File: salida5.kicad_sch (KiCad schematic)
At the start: 7 parts

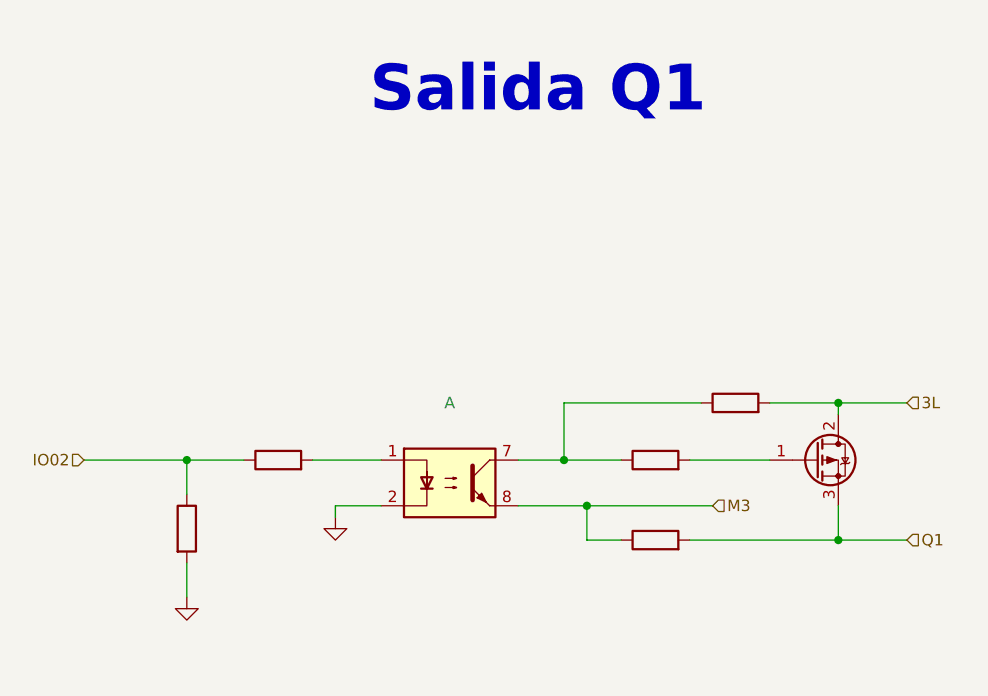
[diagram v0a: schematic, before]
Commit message: add salidas separadas 4,5,6
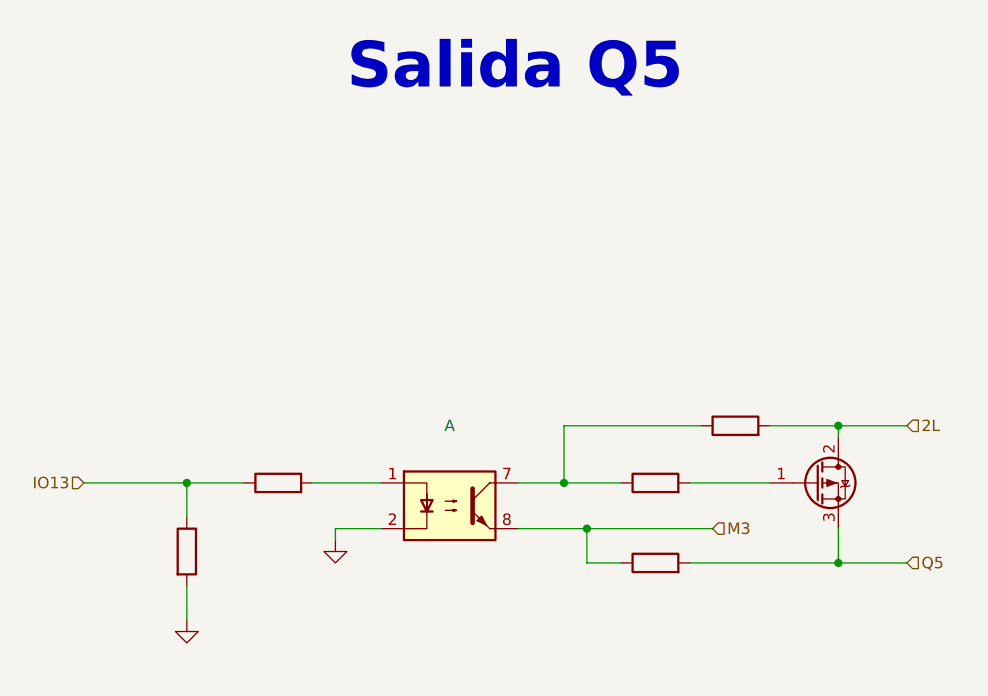
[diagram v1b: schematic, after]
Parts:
- removed ? (x5): (no value), symbol Device:R
- removed ?: (no value), symbol Transistor_FET:FQP27P06
- removed ?: (no value), symbol Isolator:ILD74
- added ? (x5): (no value), symbol Device:R
- added ?: (no value), symbol Isolator:ILD74
- added ?: (no value), symbol Transistor_FET:FQP27P06
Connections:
- net GND: now also ?.2, ?.2
- net M3: now also ?.1, ?.8
- new net: ?.1, ?.1, ?.7
- new net: ?.1, ?.2
- new net: ?.1 (G), ?.2
- new net 2L: ?.2, ?.2 (D)
- new net IO13: ?.1, ?.1
- new net Q5: ?.2, ?.3 (S)
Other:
- note added: "Salida Q5"
- note removed: "Salida Q1"

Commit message: add entradas separadas
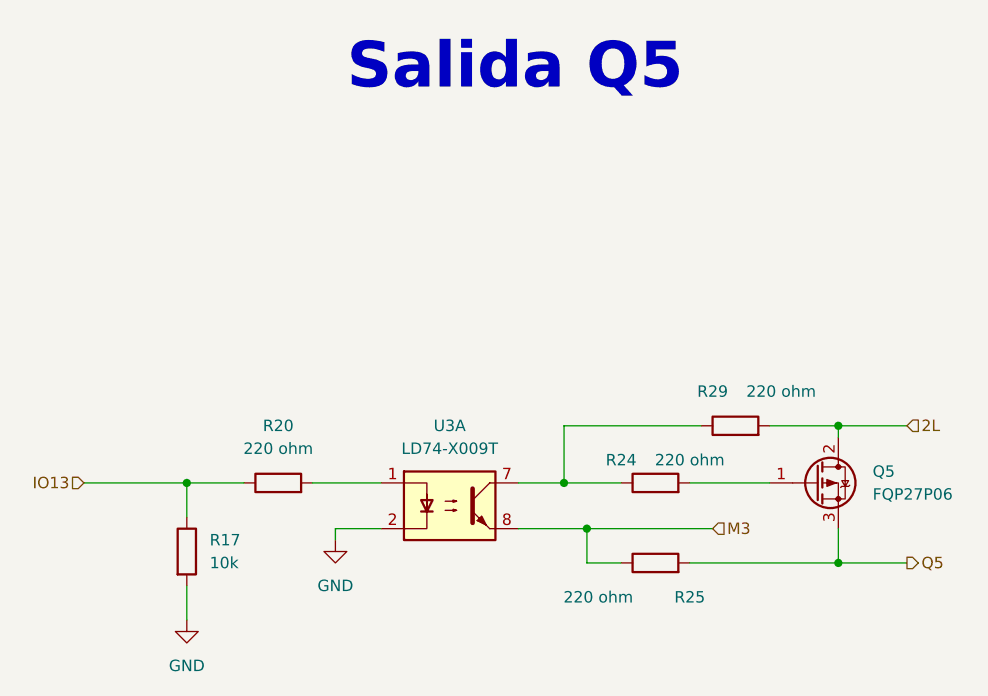
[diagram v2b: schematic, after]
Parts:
- Q5: renamed from ?; value (none) -> FQP27P06; footprint (none) -> Package_TO_SOT_SMD:TO-252-3_TabPin2
- R17: renamed from ?; value (none) -> 10k; footprint (none) -> Resistor_SMD:R_0603_1608Metric
- R20, R24, R25, R29: renamed from ?; value (none) -> 220 ohm; footprint (none) -> Resistor_SMD:R_0603_1608Metric
- U3: renamed from ?; value (none) -> LD74-X009T; footprint (none) -> Package_DIP:DIP-8_W8.89mm_SMDSocket_LongPads
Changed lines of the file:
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@@
-(kicad_sch (version 20220929) (generator eeschema)
+(kicad_sch (version 20221004) (generator eeschema)
   (paper "A4" portrait)
+  (title_block
+    (rev "José Luis Laica")
+  )
   (junction (at 140.97 115.57) (diameter 0) (color 0 0 0 0)
   )
@@
     (effects (font (size 1.27 1.27)) (justify left))
   )
-  (hierarchical_label "Q5" (shape input) (at 148.59 130.81 0) (fields_autoplaced)
+  (hierarchical_label "Q5" (shape output) (at 148.59 130.81 0) (fields_autoplaced)
     (effects (font (size 1.27 1.27)) (justify left))
   )
   (symbol (lib_id "power:GND") (at 68.58 137.16 0) (unit 1)
     (in_bom yes) (on_board yes) (dnp no) (fields_autoplaced)
-    (default_instance (reference "") (unit 1) (value "") (footprint ""))
-    (property "Reference" "" (at 68.58 143.51 0)
-      (effects (font (size 1.27 1.27)) hide)
-    )
-    (property "Value" "" (at 68.58 142.24 0)
+    (property "Reference" "#PWR012" (at 68.58 143.51 0)
+      (effects (font (size 1.27 1.27)) hide)
+    )
+    (property "Value" "GND" (at 68.58 142.24 0)
       (effects (font (size 1.27 1.27)))
     )
@@
     )
     (pin "1")
+    (instances
+      (project "PLC 32 V2"
+        (path "/d17a54f1-6eda-453f-95e1-42a53b02a1c3/64b407cd-5d00-473d-9ef6-2525490a4831"
+          (reference "#PWR012") (unit 1) (value "GND") (footprint "")
+        )
+      )
+    )
   )
   (symbol (lib_id "Device:R") (at 68.58 129.54 0) (unit 1)
     (in_bom yes) (on_board yes) (dnp no) (fields_autoplaced)
-    (default_instance (reference "") (unit 1) (value "") (footprint ""))
-    (property "Reference" "" (at 71.12 128.2699 0)
-      (effects (font (size 1.27 1.27)) (justify left))
-    )
-    (property "Value" "" (at 71.12 130.8099 0)
-      (effects (font (size 1.27 1.27)) (justify left))
-    )
-    (property "Footprint" "" (at 66.802 129.54 90)
+    (property "Reference" "R17" (at 71.12 128.2699 0)
+      (effects (font (size 1.27 1.27)) (justify left))
+    )
+    (property "Value" "10k" (at 71.12 130.8099 0)
+      (effects (font (size 1.27 1.27)) (justify left))
+    )
+    (property "Footprint" "Resistor_SMD:R_0603_1608Metric" (at 66.802 129.54 90)
       (effects (font (size 1.27 1.27)) hide)
     )
@@
     (pin "1")
     (pin "2")
+    (instances
+      (project "PLC 32 V2"
+        (path "/d17a54f1-6eda-453f-95e1-42a53b02a1c3/64b407cd-5d00-473d-9ef6-2525490a4831"
+          (reference "R17") (unit 1) (value "10k") (footprint "Resistor_SMD:R_0603_1608Metric")
+        )
+      )
+    )
   )
   (symbol (lib_id "Device:R") (at 120.65 130.81 90) (unit 1)
     (in_bom yes) (on_board yes) (dnp no)
-    (default_instance (reference "") (unit 1) (value "") (footprint ""))
-    (property "Reference" "" (at 124.46 134.62 90)
-      (effects (font (size 1.27 1.27)))
-    )
-    (property "Value" "" (at 114.3 134.62 90)
-      (effects (font (size 1.27 1.27)))
-    )
-    (property "Footprint" "" (at 120.65 132.588 90)
+    (property "Reference" "R25" (at 124.46 134.62 90)
+      (effects (font (size 1.27 1.27)))
+    )
+    (property "Value" "220 ohm" (at 114.3 134.62 90)
+      (effects (font (size 1.27 1.27)))
+    )
+    (property "Footprint" "Resistor_SMD:R_0603_1608Metric" (at 120.65 132.588 90)
       (effects (font (size 1.27 1.27)) hide)
     )
@@
     (pin "1")
     (pin "2")
+    (instances
+      (project "PLC 32 V2"
+        (path "/d17a54f1-6eda-453f-95e1-42a53b02a1c3/64b407cd-5d00-473d-9ef6-2525490a4831"
+          (reference "R25") (unit 1) (value "220 ohm") (footprint "Resistor_SMD:R_0603_1608Metric")
+        )
+      )
+    )
   )
   (symbol (lib_id "Device:R") (at 129.54 115.57 90) (unit 1)
     (in_bom yes) (on_board yes) (dnp no)
-    (default_instance (reference "") (unit 1) (value "") (footprint ""))
-    (property "Reference" "" (at 127 111.76 90)
-      (effects (font (size 1.27 1.27)))
-    )
-    (property "Value" "" (at 134.62 111.76 90)
-      (effects (font (size 1.27 1.27)))
-    )
-    (property "Footprint" "" (at 129.54 117.348 90)
+    (property "Reference" "R29" (at 127 111.76 90)
+      (effects (font (size 1.27 1.27)))
+    )
+    (property "Value" "220 ohm" (at 134.62 111.76 90)
+      (effects (font (size 1.27 1.27)))
+    )
+    (property "Footprint" "Resistor_SMD:R_0603_1608Metric" (at 129.54 117.348 90)
       (effects (font (size 1.27 1.27)) hide)
     )
@@
     (pin "1")
     (pin "2")
+    (instances
+      (project "PLC 32 V2"
+        (path "/d17a54f1-6eda-453f-95e1-42a53b02a1c3/64b407cd-5d00-473d-9ef6-2525490a4831"
+          (reference "R29") (unit 1) (value "220 ohm") (footprint "Resistor_SMD:R_0603_1608Metric")
+        )
+      )
+    )
   )
   (symbol (lib_id "Isolator:ILD74") (at 97.79 124.46 0) (unit 1)
     (in_bom yes) (on_board yes) (dnp no) (fields_autoplaced)
-    (default_instance (reference "") (unit 1) (value "") (footprint ""))
-    (property "Reference" "" (at 97.79 115.57 0)
-      (effects (font (size 1.27 1.27)))
-    )
-    (property "Value" "" (at 97.79 118.11 0)
-      (effects (font (size 1.27 1.27)))
-    )
-    (property "Footprint" "" (at 92.71 129.54 0)
+    (property "Reference" "U3" (at 97.79 115.57 0)
+      (effects (font (size 1.27 1.27)))
+    )
+    (property "Value" "LD74-X009T" (at 97.79 118.11 0)
+      (effects (font (size 1.27 1.27)))
+    )
+    (property "Footprint" "Package_DIP:DIP-8_W8.89mm_SMDSocket_LongPads" (at 92.71 129.54 0)
       (effects (font (size 1.27 1.27) italic) (justify left) hide)
     )
@@
     (pin "5")
     (pin "6")
+    (instances
+      (project "PLC 32 V2"
+        (path "/d17a54f1-6eda-453f-95e1-42a53b02a1c3/64b407cd-5d00-473d-9ef6-2525490a4831"
+          (reference "U3") (unit 1) (value "LD74-X009T") (footprint "Package_DIP:DIP-8_W8.89mm_SMDSocket_LongPads")
+        )
+      )
+    )
   )
   (symbol (lib_id "power:GND") (at 85.09 128.27 0) (unit 1)
     (in_bom yes) (on_board yes) (dnp no) (fields_autoplaced)
-    (default_instance (reference "") (unit 1) (value "") (footprint ""))
-    (property "Reference" "" (at 85.09 134.62 0)
-      (effects (font (size 1.27 1.27)) hide)
-    )
-    (property "Value" "" (at 85.09 133.35 0)
+    (property "Reference" "#PWR015" (at 85.09 134.62 0)
+      (effects (font (size 1.27 1.27)) hide)
+    )
+    (property "Value" "GND" (at 85.09 133.35 0)
       (effects (font (size 1.27 1.27)))
     )
@@
     )
     (pin "1")
+    (instances
+      (project "PLC 32 V2"
+        (path "/d17a54f1-6eda-453f-95e1-42a53b02a1c3/64b407cd-5d00-473d-9ef6-2525490a4831"
+          (reference "#PWR015") (unit 1) (value "GND") (footprint "")
+        )
+      )
+    )
   )
   (symbol (lib_id "Device:R") (at 120.65 121.92 90) (unit 1)
     (in_bom yes) (on_board yes) (dnp no)
-    (default_instance (reference "") (unit 1) (value "") (footprint ""))
-    (property "Reference" "" (at 116.84 119.38 90)
-      (effects (font (size 1.27 1.27)))
-    )
-    (property "Value" "" (at 124.46 119.38 90)
-      (effects (font (size 1.27 1.27)))
-    )
-    (property "Footprint" "" (at 120.65 123.698 90)
+    (property "Reference" "R24" (at 116.84 119.38 90)
+      (effects (font (size 1.27 1.27)))
+    )
+    (property "Value" "220 ohm" (at 124.46 119.38 90)
+      (effects (font (size 1.27 1.27)))
+    )
+    (property "Footprint" "Resistor_SMD:R_0603_1608Metric" (at 120.65 123.698 90)
       (effects (font (size 1.27 1.27)) hide)
     )
@@
     (pin "1")
     (pin "2")
+    (instances
+      (project "PLC 32 V2"
+        (path "/d17a54f1-6eda-453f-95e1-42a53b02a1c3/64b407cd-5d00-473d-9ef6-2525490a4831"
+          (reference "R24") (unit 1) (value "220 ohm") (footprint "Resistor_SMD:R_0603_1608Metric")
+        )
+      )
+    )
   )
   (symbol (lib_id "Transistor_FET:FQP27P06") (at 138.43 121.92 0) (unit 1)
     (in_bom yes) (on_board yes) (dnp no) (fields_autoplaced)
-    (default_instance (reference "") (unit 1) (value "") (footprint ""))
-    (property "Reference" "" (at 144.78 120.6499 0)
-      (effects (font (size 1.27 1.27)) (justify left))
-    )
-    (property "Value" "" (at 144.78 123.1899 0)
-      (effects (font (size 1.27 1.27)) (justify left))
-    )
-    (property "Footprint" "" (at 143.51 123.825 0)
+    (property "Reference" "Q5" (at 144.78 120.6499 0)
+      (effects (font (size 1.27 1.27)) (justify left))
+    )
+    (property "Value" "FQP27P06" (at 144.78 123.1899 0)
+      (effects (font (size 1.27 1.27)) (justify left))
+    )
+    (property "Footprint" "Package_TO_SOT_SMD:TO-252-3_TabPin2" (at 143.51 123.825 0)
       (effects (font (size 1.27 1.27) italic) (justify left) hide)
     )
@@
     (pin "2")
     (pin "3")
+    (instances
+      (project "PLC 32 V2"
+        (path "/d17a54f1-6eda-453f-95e1-42a53b02a1c3/64b407cd-5d00-473d-9ef6-2525490a4831"
+          (reference "Q5") (unit 1) (value "FQP27P06") (footprint "Package_TO_SOT_SMD:TO-252-3_TabPin2")
+        )
+      )
+    )
   )
   (symbol (lib_id "Device:R") (at 78.74 121.92 90) (unit 1)
     (in_bom yes) (on_board yes) (dnp no) (fields_autoplaced)
-    (default_instance (reference "") (unit 1) (value "") (footprint ""))
-    (property "Reference" "" (at 78.74 115.57 90)
-      (effects (font (size 1.27 1.27)))
-    )
-    (property "Value" "" (at 78.74 118.11 90)
-      (effects (font (size 1.27 1.27)))
-    )
-    (property "Footprint" "" (at 78.74 123.698 90)
+    (property "Reference" "R20" (at 78.74 115.57 90)
+      (effects (font (size 1.27 1.27)))
+    )
+    (property "Value" "220 ohm" (at 78.74 118.11 90)
+      (effects (font (size 1.27 1.27)))
+    )
+    (property "Footprint" "Resistor_SMD:R_0603_1608Metric" (at 78.74 123.698 90)
       (effects (font (size 1.27 1.27)) hide)
     )
@@
     (pin "1")
     (pin "2")
+    (instances
+      (project "PLC 32 V2"
+        (path "/d17a54f1-6eda-453f-95e1-42a53b02a1c3/64b407cd-5d00-473d-9ef6-2525490a4831"
+          (reference "R20") (unit 1) (value "220 ohm") (footprint "Resistor_SMD:R_0603_1608Metric")
+        )
+      )
+    )
   )
 )

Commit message: input/output separadas
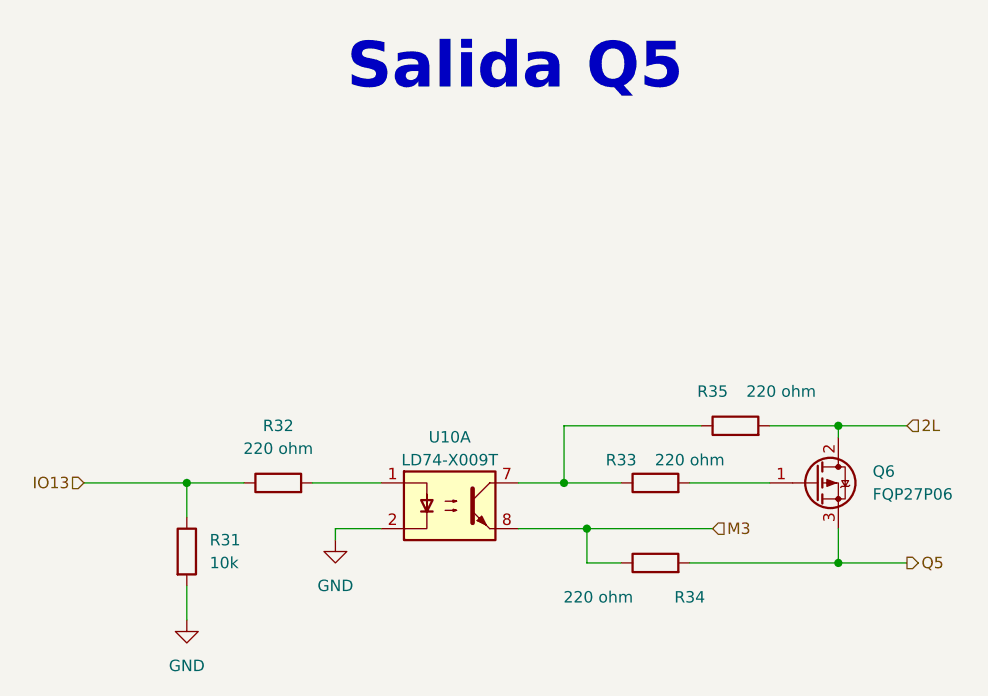
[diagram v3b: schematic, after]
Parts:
- renumbered Q5 to Q6, R17 to R31, R20 to R32, R24 to R33, R25 to R34, R29 to R35, U3 to U10
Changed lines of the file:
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@@
   (paper "A4" portrait)
   (title_block
+    (date "2022-10-09")
     (rev "José Luis Laica")
   )
@@
   (symbol (lib_id "power:GND") (at 68.58 137.16 0) (unit 1)
     (in_bom yes) (on_board yes) (dnp no) (fields_autoplaced)
-    (property "Reference" "#PWR012" (at 68.58 143.51 0)
+    (property "Reference" "#PWR020" (at 68.58 143.51 0)
       (effects (font (size 1.27 1.27)) hide)
     )
@@
       (project "PLC 32 V2"
         (path "/d17a54f1-6eda-453f-95e1-42a53b02a1c3/64b407cd-5d00-473d-9ef6-2525490a4831"
-          (reference "#PWR012") (unit 1) (value "GND") (footprint "")
+          (reference "#PWR020") (unit 1) (value "GND") (footprint "")
         )
       )
@@
   (symbol (lib_id "Device:R") (at 68.58 129.54 0) (unit 1)
     (in_bom yes) (on_board yes) (dnp no) (fields_autoplaced)
-    (property "Reference" "R17" (at 71.12 128.2699 0)
+    (property "Reference" "R31" (at 71.12 128.2699 0)
       (effects (font (size 1.27 1.27)) (justify left))
     )
@@
       (project "PLC 32 V2"
         (path "/d17a54f1-6eda-453f-95e1-42a53b02a1c3/64b407cd-5d00-473d-9ef6-2525490a4831"
-          (reference "R17") (unit 1) (value "10k") (footprint "Resistor_SMD:R_0603_1608Metric")
+          (reference "R31") (unit 1) (value "10k") (footprint "Resistor_SMD:R_0603_1608Metric")
         )
       )
@@
   (symbol (lib_id "Device:R") (at 120.65 130.81 90) (unit 1)
     (in_bom yes) (on_board yes) (dnp no)
-    (property "Reference" "R25" (at 124.46 134.62 90)
+    (property "Reference" "R34" (at 124.46 134.62 90)
       (effects (font (size 1.27 1.27)))
     )
@@
       (project "PLC 32 V2"
         (path "/d17a54f1-6eda-453f-95e1-42a53b02a1c3/64b407cd-5d00-473d-9ef6-2525490a4831"
-          (reference "R25") (unit 1) (value "220 ohm") (footprint "Resistor_SMD:R_0603_1608Metric")
+          (reference "R34") (unit 1) (value "220 ohm") (footprint "Resistor_SMD:R_0603_1608Metric")
         )
       )
@@
   (symbol (lib_id "Device:R") (at 129.54 115.57 90) (unit 1)
     (in_bom yes) (on_board yes) (dnp no)
-    (property "Reference" "R29" (at 127 111.76 90)
+    (property "Reference" "R35" (at 127 111.76 90)
       (effects (font (size 1.27 1.27)))
     )
@@
       (project "PLC 32 V2"
         (path "/d17a54f1-6eda-453f-95e1-42a53b02a1c3/64b407cd-5d00-473d-9ef6-2525490a4831"
-          (reference "R29") (unit 1) (value "220 ohm") (footprint "Resistor_SMD:R_0603_1608Metric")
+          (reference "R35") (unit 1) (value "220 ohm") (footprint "Resistor_SMD:R_0603_1608Metric")
         )
       )
@@
   (symbol (lib_id "Isolator:ILD74") (at 97.79 124.46 0) (unit 1)
     (in_bom yes) (on_board yes) (dnp no) (fields_autoplaced)
-    (property "Reference" "U3" (at 97.79 115.57 0)
-      (effects (font (size 1.27 1.27)))
-    )
-    (property "Value" "LD74-X009T" (at 97.79 118.11 0)
+    (property "Reference" "U10" (at 97.79 116.84 0)
+      (effects (font (size 1.27 1.27)))
+    )
+    (property "Value" "LD74-X009T" (at 97.79 119.38 0)
       (effects (font (size 1.27 1.27)))
     )
@@
       (project "PLC 32 V2"
         (path "/d17a54f1-6eda-453f-95e1-42a53b02a1c3/64b407cd-5d00-473d-9ef6-2525490a4831"
-          (reference "U3") (unit 1) (value "LD74-X009T") (footprint "Package_DIP:DIP-8_W8.89mm_SMDSocket_LongPads")
+          (reference "U10") (unit 1) (value "LD74-X009T") (footprint "Package_DIP:DIP-8_W8.89mm_SMDSocket_LongPads")
         )
       )
@@
   (symbol (lib_id "power:GND") (at 85.09 128.27 0) (unit 1)
     (in_bom yes) (on_board yes) (dnp no) (fields_autoplaced)
-    (property "Reference" "#PWR015" (at 85.09 134.62 0)
+    (property "Reference" "#PWR021" (at 85.09 134.62 0)
       (effects (font (size 1.27 1.27)) hide)
     )
@@
       (project "PLC 32 V2"
         (path "/d17a54f1-6eda-453f-95e1-42a53b02a1c3/64b407cd-5d00-473d-9ef6-2525490a4831"
-          (reference "#PWR015") (unit 1) (value "GND") (footprint "")
+          (reference "#PWR021") (unit 1) (value "GND") (footprint "")
         )
       )
@@
   (symbol (lib_id "Device:R") (at 120.65 121.92 90) (unit 1)
     (in_bom yes) (on_board yes) (dnp no)
-    (property "Reference" "R24" (at 116.84 119.38 90)
+    (property "Reference" "R33" (at 116.84 119.38 90)
       (effects (font (size 1.27 1.27)))
     )
@@
       (project "PLC 32 V2"
         (path "/d17a54f1-6eda-453f-95e1-42a53b02a1c3/64b407cd-5d00-473d-9ef6-2525490a4831"
-          (reference "R24") (unit 1) (value "220 ohm") (footprint "Resistor_SMD:R_0603_1608Metric")
+          (reference "R33") (unit 1) (value "220 ohm") (footprint "Resistor_SMD:R_0603_1608Metric")
         )
       )
@@
   (symbol (lib_id "Transistor_FET:FQP27P06") (at 138.43 121.92 0) (unit 1)
     (in_bom yes) (on_board yes) (dnp no) (fields_autoplaced)
-    (property "Reference" "Q5" (at 144.78 120.6499 0)
+    (property "Reference" "Q6" (at 144.78 120.6499 0)
       (effects (font (size 1.27 1.27)) (justify left))
     )
@@
       (project "PLC 32 V2"
         (path "/d17a54f1-6eda-453f-95e1-42a53b02a1c3/64b407cd-5d00-473d-9ef6-2525490a4831"
-          (reference "Q5") (unit 1) (value "FQP27P06") (footprint "Package_TO_SOT_SMD:TO-252-3_TabPin2")
+          (reference "Q6") (unit 1) (value "FQP27P06") (footprint "Package_TO_SOT_SMD:TO-252-3_TabPin2")
         )
       )
@@
   (symbol (lib_id "Device:R") (at 78.74 121.92 90) (unit 1)
     (in_bom yes) (on_board yes) (dnp no) (fields_autoplaced)
-    (property "Reference" "R20" (at 78.74 115.57 90)
+    (property "Reference" "R32" (at 78.74 115.57 90)
       (effects (font (size 1.27 1.27)))
     )
@@
       (project "PLC 32 V2"
         (path "/d17a54f1-6eda-453f-95e1-42a53b02a1c3/64b407cd-5d00-473d-9ef6-2525490a4831"
-          (reference "R20") (unit 1) (value "220 ohm") (footprint "Resistor_SMD:R_0603_1608Metric")
-        )
-      )
+          (reference "R32") (unit 1) (value "220 ohm") (footprint "Resistor_SMD:R_0603_1608Metric")
+        )
+      )
